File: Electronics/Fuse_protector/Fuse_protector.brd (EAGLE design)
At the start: 59.7 x 39.4 mm, 12 parts

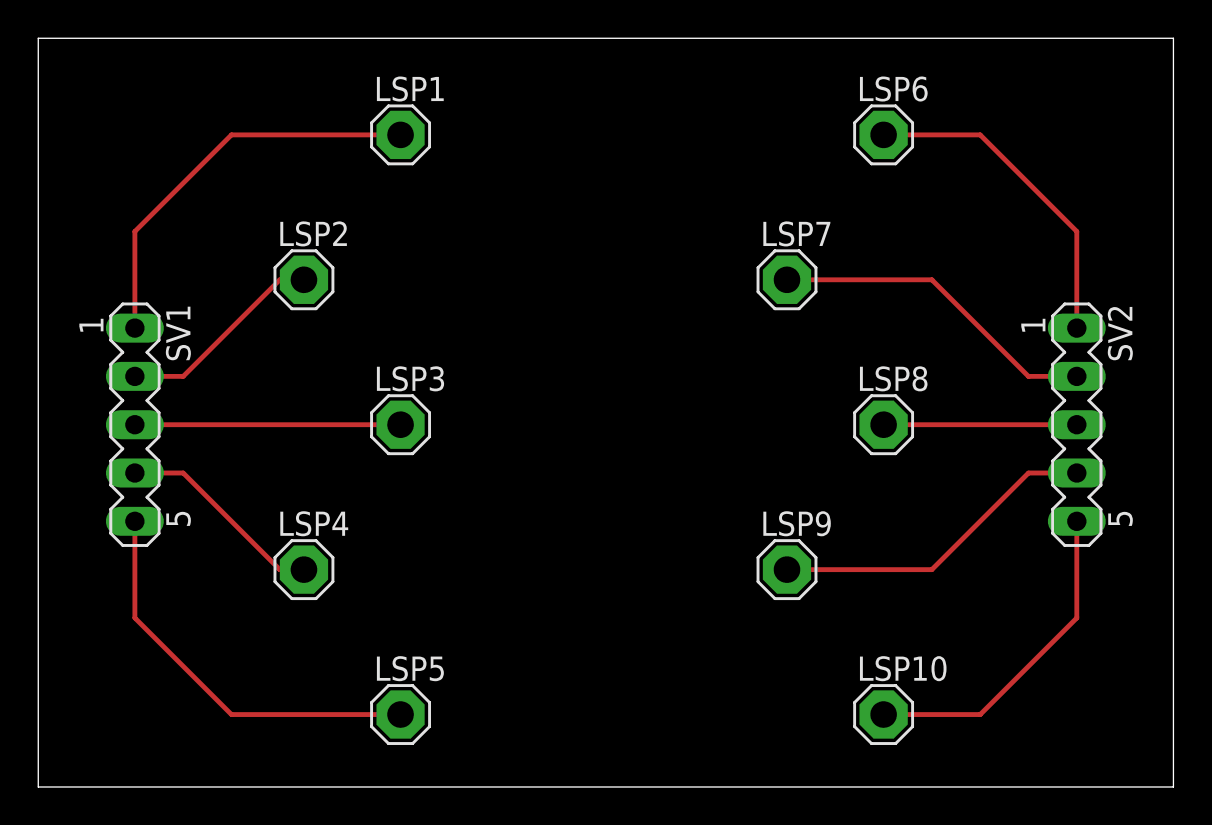
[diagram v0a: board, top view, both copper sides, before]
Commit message: Fuse protector improved
What has been improved:
- corrected size of space for fuses
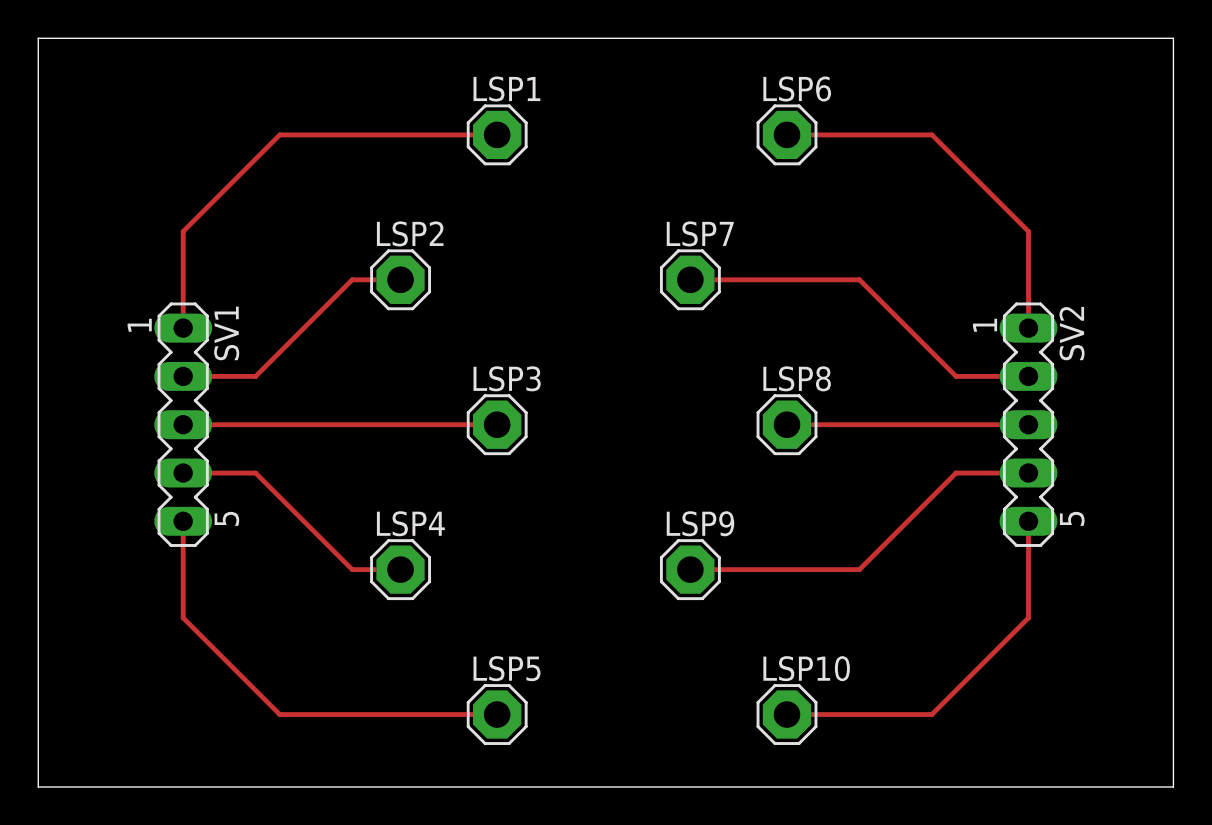
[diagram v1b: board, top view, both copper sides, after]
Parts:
- moved LSP10 5.08 mm to (39.4, 3.81)
- moved LSP6 5.08 mm to (39.4, 34.3)
- moved LSP8 5.08 mm to (39.4, 19.1)
- moved LSP2 5.08 mm to (19.1, 26.7)
- moved LSP4 5.08 mm to (19.1, 11.4)
- moved LSP1 5.08 mm to (24.1, 34.3)
- moved LSP3 5.08 mm to (24.1, 19.1)
- moved LSP5 5.08 mm to (24.1, 3.81)
- moved LSP7 5.08 mm to (34.3, 26.7)
- moved LSP9 5.08 mm to (34.3, 11.4)
- moved SV1 2.54 mm to (7.62, 19.1)
- moved SV2 2.54 mm to (52.1, 19.1)
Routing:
- net N$8: track 10.2 -> 12.7 mm
- net N$6: track 17.3 -> 19.9 mm
- net N$10: track 17.3 -> 19.9 mm
- net N$4: track 11.0 -> 13.5 mm
- net N$2: track 11.0 -> 13.5 mm
- net N$9: track 17.3 -> 19.9 mm
- net N$7: track 17.3 -> 19.9 mm
- net N$3: track 14.0 -> 16.5 mm
- net N$5: track 21.2 -> 23.7 mm
- net N$1: track 21.2 -> 23.7 mm
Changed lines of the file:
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@@
 <dimension x1="0" y1="39.37" x2="0" y2="0" x3="-3.81" y3="19.685" textsize="1.778" layer="47"/>
 <dimension x1="0" y1="0" x2="59.69" y2="0" x3="29.845" y3="-3.81" textsize="1.778" layer="47"/>
+<dimension x1="24.13" y1="3.81" x2="39.37" y2="3.81" x3="31.75" y3="-7.62" textsize="1.778" layer="47"/>
 </plain>
 <attributes>
@@
 </autorouter>
 <elements>
-<element name="LSP1" library="solpad" package="SE14" value="SE14" x="19.05" y="34.29"/>
-<element name="LSP10" library="solpad" package="SE14" value="SE14" x="44.45" y="3.81"/>
-<element name="LSP2" library="solpad" package="SE14" value="SE14" x="13.97" y="26.67"/>
-<element name="LSP3" library="solpad" package="SE14" value="SE14" x="19.05" y="19.05"/>
-<element name="LSP4" library="solpad" package="SE14" value="SE14" x="13.97" y="11.43"/>
-<element name="LSP5" library="solpad" package="SE14" value="SE14" x="19.05" y="3.81"/>
-<element name="LSP6" library="solpad" package="SE14" value="SE14" x="44.45" y="34.29"/>
-<element name="LSP7" library="solpad" package="SE14" value="SE14" x="39.37" y="26.67"/>
-<element name="LSP8" library="solpad" package="SE14" value="SE14" x="44.45" y="19.05"/>
-<element name="LSP9" library="solpad" package="SE14" value="SE14" x="39.37" y="11.43"/>
-<element name="SV1" library="con-lstb" package="MA05-1" value="SV1" x="5.08" y="19.05" rot="R270">
-<attribute name="MF" value="" x="5.08" y="19.05" size="1.778" layer="27" rot="R270" display="off"/>
-<attribute name="MPN" value="" x="5.08" y="19.05" size="1.778" layer="27" rot="R270" display="off"/>
-<attribute name="OC_FARNELL" value="unknown" x="5.08" y="19.05" size="1.778" layer="27" rot="R270" display="off"/>
-<attribute name="OC_NEWARK" value="unknown" x="5.08" y="19.05" size="1.778" layer="27" rot="R270" display="off"/>
+<element name="LSP1" library="solpad" package="SE14" value="SE14" x="24.13" y="34.29"/>
+<element name="LSP10" library="solpad" package="SE14" value="SE14" x="39.37" y="3.81"/>
+<element name="LSP2" library="solpad" package="SE14" value="SE14" x="19.05" y="26.67"/>
+<element name="LSP3" library="solpad" package="SE14" value="SE14" x="24.13" y="19.05"/>
+<element name="LSP4" library="solpad" package="SE14" value="SE14" x="19.05" y="11.43"/>
+<element name="LSP5" library="solpad" package="SE14" value="SE14" x="24.13" y="3.81"/>
+<element name="LSP6" library="solpad" package="SE14" value="SE14" x="39.37" y="34.29"/>
+<element name="LSP7" library="solpad" package="SE14" value="SE14" x="34.29" y="26.67"/>
+<element name="LSP8" library="solpad" package="SE14" value="SE14" x="39.37" y="19.05"/>
+<element name="LSP9" library="solpad" package="SE14" value="SE14" x="34.29" y="11.43"/>
+<element name="SV1" library="con-lstb" package="MA05-1" value="SV1" x="7.62" y="19.05" rot="R270">
+<attribute name="MF" value="" x="7.62" y="19.05" size="1.778" layer="27" rot="R270" display="off"/>
+<attribute name="MPN" value="" x="7.62" y="19.05" size="1.778" layer="27" rot="R270" display="off"/>
+<attribute name="OC_FARNELL" value="unknown" x="7.62" y="19.05" size="1.778" layer="27" rot="R270" display="off"/>
+<attribute name="OC_NEWARK" value="unknown" x="7.62" y="19.05" size="1.778" layer="27" rot="R270" display="off"/>
 </element>
-<element name="SV2" library="con-lstb" package="MA05-1" value="SV2" x="54.61" y="19.05" rot="R270">
-<attribute name="MF" value="" x="54.61" y="19.05" size="1.778" layer="27" rot="R270" display="off"/>
-<attribute name="MPN" value="" x="54.61" y="19.05" size="1.778" layer="27" rot="R270" display="off"/>
-<attribute name="OC_FARNELL" value="unknown" x="54.61" y="19.05" size="1.778" layer="27" rot="R270" display="off"/>
-<attribute name="OC_NEWARK" value="unknown" x="54.61" y="19.05" size="1.778" layer="27" rot="R270" display="off"/>
+<element name="SV2" library="con-lstb" package="MA05-1" value="SV2" x="52.07" y="19.05" rot="R270">
+<attribute name="MF" value="" x="52.07" y="19.05" size="1.778" layer="27" rot="R270" display="off"/>
+<attribute name="MPN" value="" x="52.07" y="19.05" size="1.778" layer="27" rot="R270" display="off"/>
+<attribute name="OC_FARNELL" value="unknown" x="52.07" y="19.05" size="1.778" layer="27" rot="R270" display="off"/>
+<attribute name="OC_NEWARK" value="unknown" x="52.07" y="19.05" size="1.778" layer="27" rot="R270" display="off"/>
 </element>
 </elements>
@@
 <contactref element="LSP1" pad="MP"/>
 <contactref element="SV1" pad="1"/>
-<wire x1="5.08" y1="24.13" x2="5.08" y2="29.21" width="0.254" layer="1"/>
-<wire x1="5.08" y1="29.21" x2="10.16" y2="34.29" width="0.254" layer="1"/>
-<wire x1="10.16" y1="34.29" x2="19.05" y2="34.29" width="0.254" layer="1"/>
+<wire x1="7.62" y1="24.13" x2="7.62" y2="29.21" width="0.254" layer="1"/>
+<wire x1="7.62" y1="29.21" x2="12.7" y2="34.29" width="0.254" layer="1"/>
+<wire x1="12.7" y1="34.29" x2="24.13" y2="34.29" width="0.254" layer="1"/>
 </signal>
 <signal name="N$2">
 <contactref element="LSP2" pad="MP"/>
 <contactref element="SV1" pad="2"/>
-<wire x1="5.08" y1="21.59" x2="7.62" y2="21.59" width="0.254" layer="1"/>
-<wire x1="7.62" y1="21.59" x2="12.7" y2="26.67" width="0.254" layer="1"/>
-<wire x1="12.7" y1="26.67" x2="13.97" y2="26.67" width="0.254" layer="1"/>
+<wire x1="7.62" y1="21.59" x2="11.43" y2="21.59" width="0.254" layer="1"/>
+<wire x1="11.43" y1="21.59" x2="16.51" y2="26.67" width="0.254" layer="1"/>
+<wire x1="16.51" y1="26.67" x2="19.05" y2="26.67" width="0.254" layer="1"/>
 </signal>
 <signal name="N$4">
 <contactref element="LSP4" pad="MP"/>
 <contactref element="SV1" pad="4"/>
-<wire x1="5.08" y1="16.51" x2="7.62" y2="16.51" width="0.254" layer="1"/>
-<wire x1="7.62" y1="16.51" x2="12.7" y2="11.43" width="0.254" layer="1"/>
-<wire x1="12.7" y1="11.43" x2="13.97" y2="11.43" width="0.254" layer="1"/>
+<wire x1="7.62" y1="16.51" x2="11.43" y2="16.51" width="0.254" layer="1"/>
+<wire x1="11.43" y1="16.51" x2="16.51" y2="11.43" width="0.254" layer="1"/>
+<wire x1="16.51" y1="11.43" x2="19.05" y2="11.43" width="0.254" layer="1"/>
 </signal>
 <signal name="N$5">
 <contactref element="LSP5" pad="MP"/>
 <contactref element="SV1" pad="5"/>
-<wire x1="5.08" y1="13.97" x2="5.08" y2="8.89" width="0.254" layer="1"/>
-<wire x1="5.08" y1="8.89" x2="10.16" y2="3.81" width="0.254" layer="1"/>
-<wire x1="10.16" y1="3.81" x2="19.05" y2="3.81" width="0.254" layer="1"/>
+<wire x1="7.62" y1="13.97" x2="7.62" y2="8.89" width="0.254" layer="1"/>
+<wire x1="7.62" y1="8.89" x2="12.7" y2="3.81" width="0.254" layer="1"/>
+<wire x1="12.7" y1="3.81" x2="24.13" y2="3.81" width="0.254" layer="1"/>
 </signal>
 <signal name="N$6">
 <contactref element="SV2" pad="1"/>
 <contactref element="LSP6" pad="MP"/>
-<wire x1="54.61" y1="24.13" x2="54.61" y2="29.21" width="0.254" layer="1"/>
-<wire x1="54.61" y1="29.21" x2="49.53" y2="34.29" width="0.254" layer="1"/>
-<wire x1="49.53" y1="34.29" x2="44.45" y2="34.29" width="0.254" layer="1"/>
+<wire x1="52.07" y1="24.13" x2="52.07" y2="29.21" width="0.254" layer="1"/>
+<wire x1="52.07" y1="29.21" x2="46.99" y2="34.29" width="0.254" layer="1"/>
+<wire x1="46.99" y1="34.29" x2="39.37" y2="34.29" width="0.254" layer="1"/>
 </signal>
 <signal name="N$7">
 <contactref element="SV2" pad="2"/>
 <contactref element="LSP7" pad="MP"/>
-<wire x1="54.61" y1="21.59" x2="52.07" y2="21.59" width="0.254" layer="1"/>
-<wire x1="52.07" y1="21.59" x2="46.99" y2="26.67" width="0.254" layer="1"/>
-<wire x1="46.99" y1="26.67" x2="39.37" y2="26.67" width="0.254" layer="1"/>
+<wire x1="52.07" y1="21.59" x2="48.26" y2="21.59" width="0.254" layer="1"/>
+<wire x1="43.18" y1="26.67" x2="34.29" y2="26.67" width="0.254" layer="1"/>
+<wire x1="43.18" y1="26.67" x2="48.26" y2="21.59" width="0.254" layer="1"/>
 </signal>
 <signal name="N$8">
 <contactref element="SV2" pad="3"/>
 <contactref element="LSP8" pad="MP"/>
-<wire x1="54.61" y1="19.05" x2="44.45" y2="19.05" width="0.254" layer="1"/>
+<wire x1="52.07" y1="19.05" x2="39.37" y2="19.05" width="0.254" layer="1"/>
 </signal>
 <signal name="N$9">
 <contactref element="SV2" pad="4"/>
 <contactref element="LSP9" pad="MP"/>
-<wire x1="54.61" y1="16.51" x2="52.07" y2="16.51" width="0.254" layer="1"/>
-<wire x1="52.07" y1="16.51" x2="46.99" y2="11.43" width="0.254" layer="1"/>
-<wire x1="46.99" y1="11.43" x2="39.37" y2="11.43" width="0.254" layer="1"/>
+<wire x1="52.07" y1="16.51" x2="48.26" y2="16.51" width="0.254" layer="1"/>
+<wire x1="43.18" y1="11.43" x2="34.29" y2="11.43" width="0.254" layer="1"/>
+<wire x1="43.18" y1="11.43" x2="48.26" y2="16.51" width="0.254" layer="1"/>
 </signal>
 <signal name="N$10">
 <contactref element="SV2" pad="5"/>
 <contactref element="LSP10" pad="MP"/>
-<wire x1="54.61" y1="13.97" x2="54.61" y2="8.89" width="0.254" layer="1"/>
-<wire x1="54.61" y1="8.89" x2="49.53" y2="3.81" width="0.254" layer="1"/>
-<wire x1="49.53" y1="3.81" x2="44.45" y2="3.81" width="0.254" layer="1"/>
+<wire x1="52.07" y1="13.97" x2="52.07" y2="8.89" width="0.254" layer="1"/>
+<wire x1="52.07" y1="8.89" x2="46.99" y2="3.81" width="0.254" layer="1"/>
+<wire x1="46.99" y1="3.81" x2="39.37" y2="3.81" width="0.254" layer="1"/>
 </signal>
 <signal name="N$3">
 <contactref element="LSP3" pad="MP"/>
 <contactref element="SV1" pad="3"/>
-<wire x1="5.08" y1="19.05" x2="19.05" y2="19.05" width="0.254" layer="1"/>
+<wire x1="7.62" y1="19.05" x2="24.13" y2="19.05" width="0.254" layer="1"/>
 </signal>
 </signals>
